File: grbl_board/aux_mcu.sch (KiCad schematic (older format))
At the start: 52 parts, among them J17 USB_B, J18 ICSP, Q5 BSS127S, Q6 BSS127S, Q7 BSS127S, SW2 SW_Push, U25 FT231XS, U26 40106, U27 74LS155, U28 ATmega328P-AU, U29 74LS153, U30 74LS153, Y2 16M

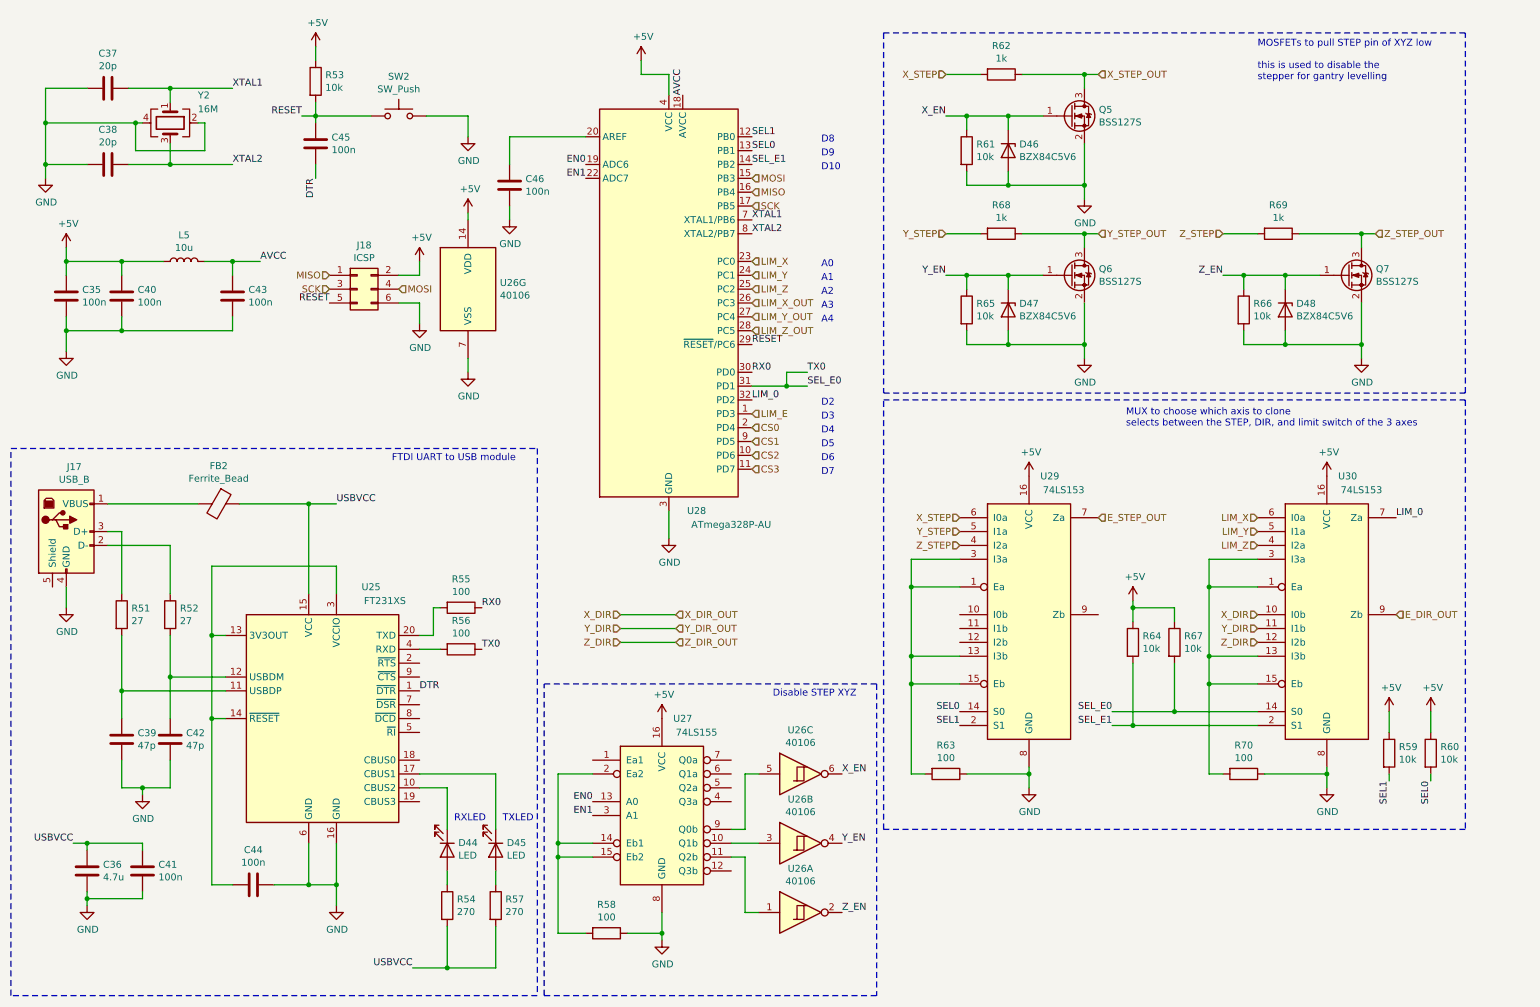
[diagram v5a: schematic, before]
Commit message: updated board with 24V reg
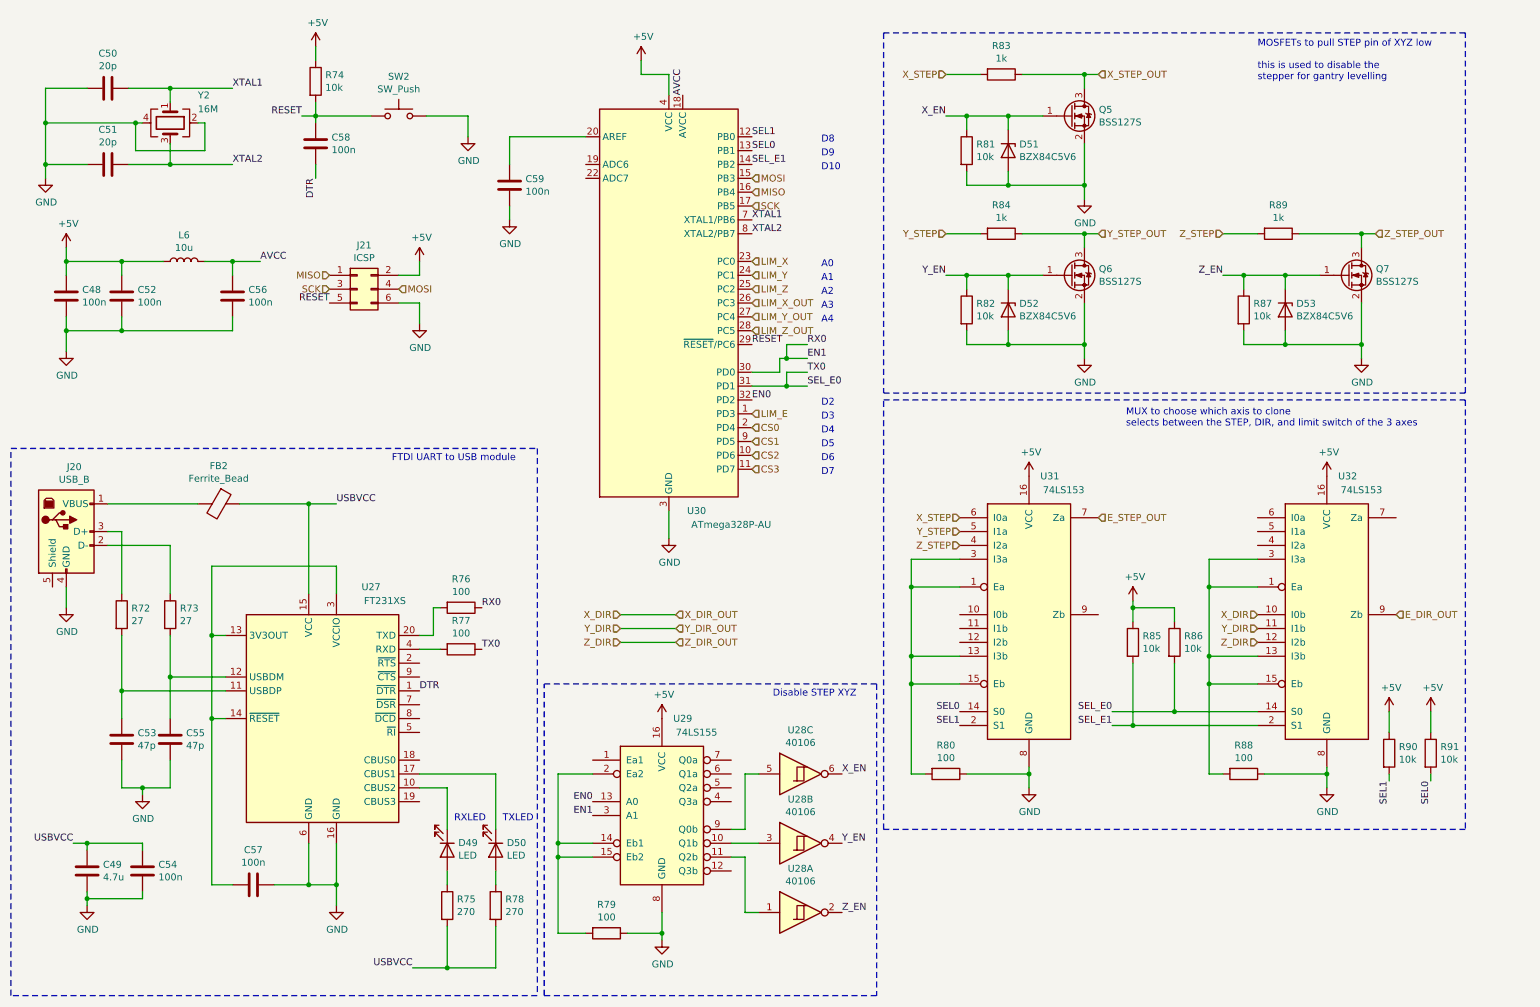
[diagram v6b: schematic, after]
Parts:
- removed unit 7 of U26
- renumbered C35 to C48, C36 to C49, C37 to C50, C38 to C51, C40 to C52, C39 to C53, C41 to C54, C42 to C55, C43 to C56, C44 to C57, C45 to C58, C46 to C59, D44 to D49, D45 to D50, D46 to D51, D47 to D52, D48 to D53, J17 to J20, J18 to J21, L5 to L6, R51 to R72, R52 to R73, R53 to R74, R54 to R75, R55 to R76, R56 to R77, R57 to R78, R58 to R79, R63 to R80, R61 to R81, R65 to R82, R62 to R83, R68 to R84, R64 to R85, R67 to R86, R66 to R87, R70 to R88, R69 to R89, R59 to R90, R60 to R91, U25 to U27, U26 to U28, U27 to U29, U28 to U30, U29 to U31, U30 to U32
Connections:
- net RX0 is gone; now on net EN1: R76.1, U30.30 (PD0)
- net EN0: now also U30.32 (PD2); no longer U30.19 (ADC6)
- net EN1: no longer U30.22 (ADC7)
- net LIM_X: no longer U32.6 (I0a)
- net LIM_Y: no longer U32.5 (I1a)
- net LIM_Z: no longer U32.4 (I2a)
- net LIM_0: no longer names the net of U32.7 (Za)
- net LIM_0: no longer U30.32 (PD2)
